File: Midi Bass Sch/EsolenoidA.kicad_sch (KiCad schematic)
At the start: 105 parts, among them Q10 BDW93C, Q11 BDW93C, Q12 BDW93C, Q13 BDW93C, Q14 BDW93C, Q15 BDW93C, Q16 BDW93C, Q17 BDW93C, Q18 BDW93C, Q19 BDW93C, Q20 BDW93C, Q21 BDW93C, Q22 BDW93C, Q23 BDW93C, Q24 BDW93C, Q25 BDW93C, Q26 BDW93C, Q27 BDW93C, Q28 BDW93C, Q9 BDW93C, U10 LTV-247, U11 LTV-247, U12 LTV-247, U13 LTV-247, U9 LTV-247

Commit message: working on troubleshooting section of report
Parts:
- renumbered L9 to L13, L10 to L14, L11 to L15, L12 to L16, L13 to L17, L14 to L18, L15 to L19, L16 to L20, L17 to L21, L18 to L22, L19 to L23, L20 to L24, L21 to L25, L22 to L26, L23 to L27, L24 to L28, L25 to L29, L26 to L30, L27 to L31, L28 to L32, Q9 to Q13, Q10 to Q14, Q11 to Q15, Q12 to Q16, Q13 to Q17, Q14 to Q18, Q15 to Q19, Q16 to Q20, Q17 to Q21, Q18 to Q22, Q19 to Q23, Q20 to Q24, Q21 to Q25, Q22 to Q26, Q23 to Q27, Q24 to Q28, Q25 to Q29, Q26 to Q30, Q27 to Q31, Q28 to Q32, R88 to R100, R89 to R101, R90 to R102, R91 to R103, R92 to R104, R93 to R105, R94 to R106, R95 to R107, R96 to R108, R97 to R109, R98 to R110, R99 to R111, R100 to R112, R101 to R113, R102 to R114, R103 to R115, R104 to R116, R105 to R117, R106 to R118, R107 to R119, R108 to R120, R109 to R121, R110 to R122, R111 to R123, R112 to R124, R113 to R125, R114 to R126, R115 to R127, R116 to R128, R117 to R129, R58 to R70, R59 to R71, R60 to R72, R61 to R73, R62 to R74, R63 to R75, R64 to R76, R65 to R77, R66 to R78, R67 to R79, R68 to R80, R69 to R81, R70 to R82, R71 to R83, R72 to R84, R73 to R85, R74 to R86, R75 to R87, R76 to R88, R77 to R89, R78 to R90, R79 to R91, R80 to R92, R81 to R93, R82 to R94, R83 to R95, R84 to R96, R85 to R97, R86 to R98, R87 to R99, U9 to U11, U10 to U12, U11 to U13, U12 to U14, U13 to U15

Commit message: changed transistor for schematic
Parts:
- Q13, Q14, Q15, Q16, Q17, Q18, Q19, Q20, Q21, Q22, Q23, Q24, Q25, Q26, Q27, Q28, Q29, Q30, Q31, Q32: value BDW93C -> STN851-A
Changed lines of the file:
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@@
 			)
 		)
-		(property "Value" "BDW93C"
+		(property "Value" "STN851-A"
 			(at 119.38 97.7899 0)
 			(effects
@@
 			)
 		)
-		(property "Value" "BDW93C"
+		(property "Value" "STN851-A"
 			(at 119.38 67.3099 0)
 			(effects
@@
 			)
 		)
-		(property "Value" "BDW93C"
+		(property "Value" "STN851-A"
 			(at 118.11 191.7699 0)
 			(effects
@@
 			)
 		)
-		(property "Value" "BDW93C"
+		(property "Value" "STN851-A"
 			(at 172.72 132.0799 0)
 			(effects
@@
 			)
 		)
-		(property "Value" "BDW93C"
+		(property "Value" "STN851-A"
 			(at 64.77 35.5599 0)
 			(effects
@@
 			)
 		)
-		(property "Value" "BDW93C"
+		(property "Value" "STN851-A"
 			(at 172.72 99.0599 0)
 			(effects
@@
 			)
 		)
-		(property "Value" "BDW93C"
+		(property "Value" "STN851-A"
 			(at 236.22 68.5799 0)
 			(effects
@@
 			)
 		)
-		(property "Value" "BDW93C"
+		(property "Value" "STN851-A"
 			(at 62.23 132.0799 0)
 			(effects
@@
 			)
 		)
-		(property "Value" "BDW93C"
+		(property "Value" "STN851-A"
 			(at 118.11 128.2699 0)
 			(effects
@@
 			)
 		)
-		(property "Value" "BDW93C"
+		(property "Value" "STN851-A"
 			(at 119.38 35.5599 0)
 			(effects
@@
 			)
 		)
-		(property "Value" "BDW93C"
+		(property "Value" "STN851-A"
 			(at 172.72 36.8299 0)
 			(effects
@@
 			)
 		)
-		(property "Value" "BDW93C"
+		(property "Value" "STN851-A"
 			(at 118.11 161.2899 0)
 			(effects
@@
 			)
 		)
-		(property "Value" "BDW93C"
+		(property "Value" "STN851-A"
 			(at 237.49 133.3499 0)
 			(effects
@@
 			)
 		)
-		(property "Value" "BDW93C"
+		(property "Value" "STN851-A"
 			(at 172.72 68.5799 0)
 			(effects
@@
 			)
 		)
-		(property "Value" "BDW93C"
+		(property "Value" "STN851-A"
 			(at 236.22 36.8299 0)
 			(effects
@@
 			)
 		)
-		(property "Value" "BDW93C"
+		(property "Value" "STN851-A"
 			(at 62.23 100.3299 0)
 			(effects
@@
 			)
 		)
-		(property "Value" "BDW93C"
+		(property "Value" "STN851-A"
 			(at 63.5 68.5799 0)
 			(effects
@@
 			)
 		)
-		(property "Value" "BDW93C"
+		(property "Value" "STN851-A"
 			(at 236.22 99.0599 0)
 			(effects
@@
 			)
 		)
-		(property "Value" "BDW93C"
+		(property "Value" "STN851-A"
 			(at 62.23 163.8299 0)
 			(effects
@@
 			)
 		)
-		(property "Value" "BDW93C"
+		(property "Value" "STN851-A"
 			(at 60.96 194.3099 0)
 			(effects

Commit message: began getting images for schematic appendix
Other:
- title: (none) -> E-slave Solenoid Array
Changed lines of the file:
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@@
 	(generator_version "8.0")
 	(paper "A")
+	(title_block
+		(title "E-slave Solenoid Array")
+		(date "2024-12-10")
+		(rev "A")
+	)
 	(junction
 		(at 233.68 54.61)

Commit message: began working on pcb layout deleted extra schematics for solenoid break out board
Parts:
- L13, L14, L15, L16, L17, L18, L19, L20, L21, L22, L23, L24, L25, L26, L27, L28, L29, L30, L31, L32: footprint (none) -> Connector_PinHeader_2.54mm:PinHeader_1x02_P2.54mm_Vertical

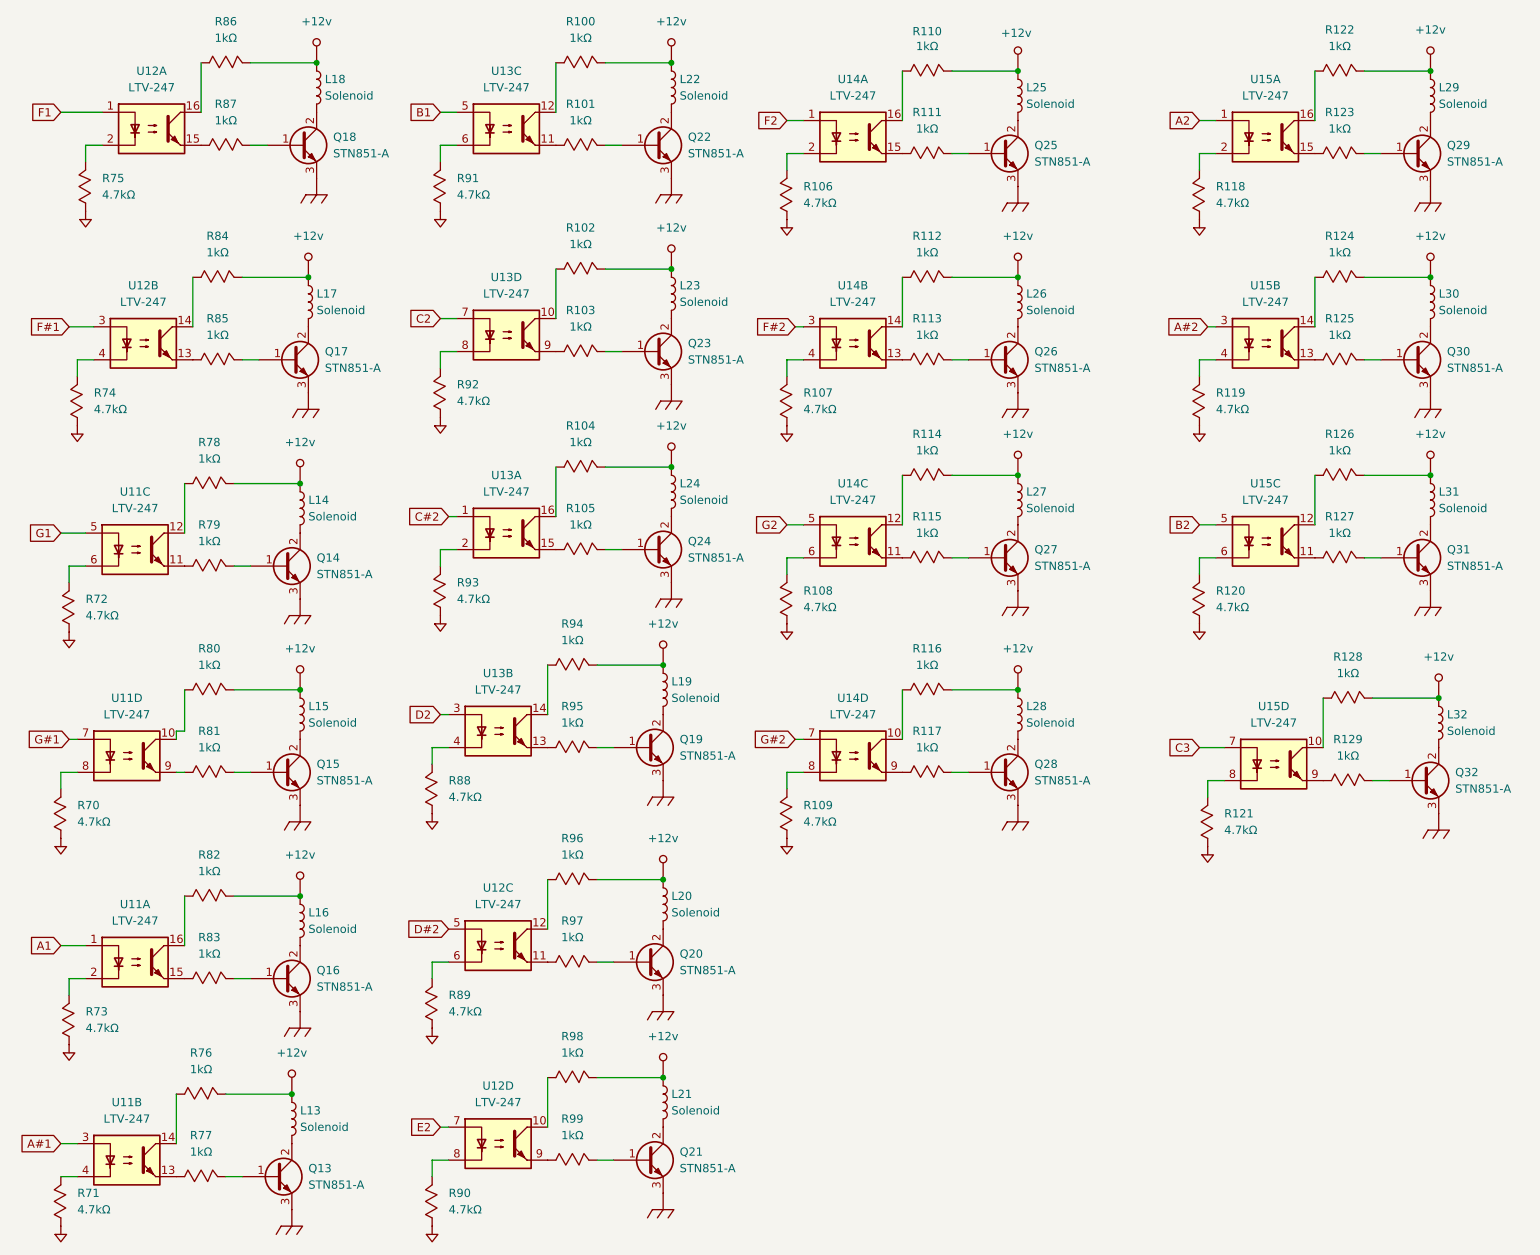
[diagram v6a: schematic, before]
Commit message: changed solenoid schematic to include LED indicators
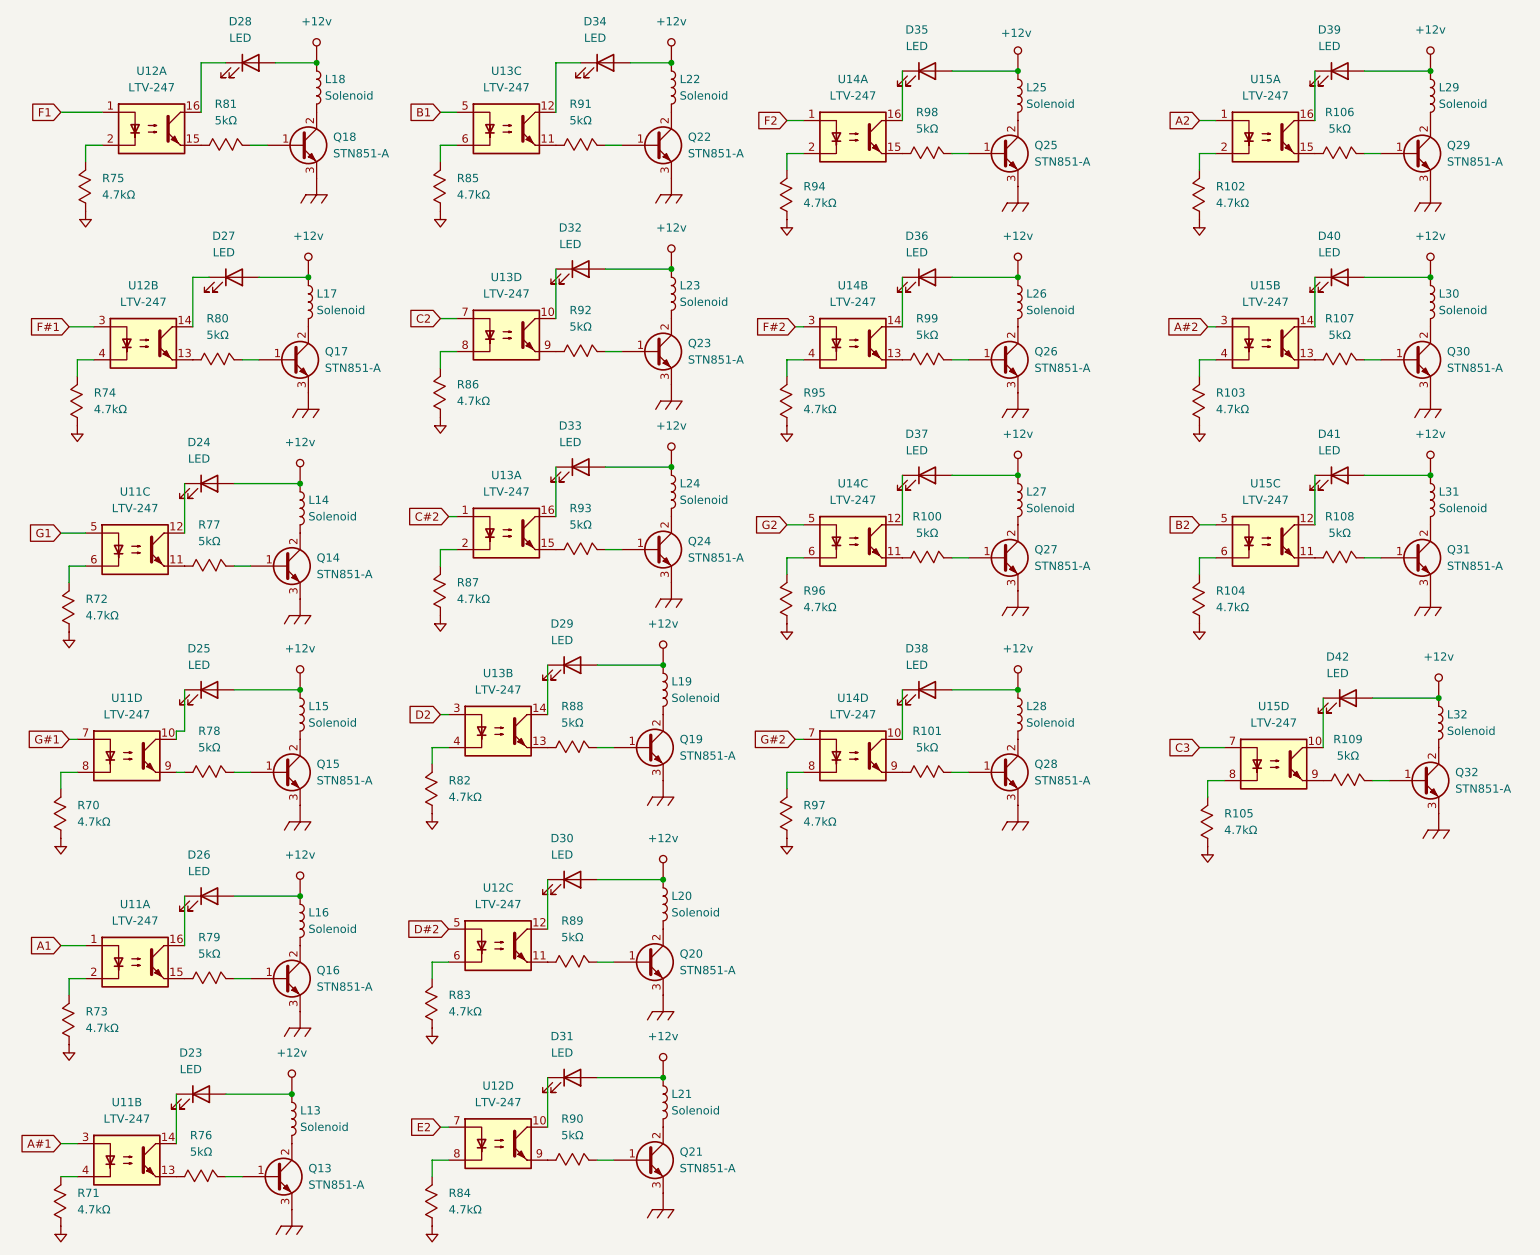
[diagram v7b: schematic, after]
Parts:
- removed R100, R102, R104, R110, R112, R114, R116, R122, R124, R126, R128, R76, R78, R80, R82, R84, R86, R94, R96, R98: 1kΩ, Resistor_SMD:R_0805_2012Metric_Pad1.20x1.40mm_HandSolder, symbol Custom Symbols:Resistor_Mod
- added D23, D24, D25, D26, D27, D28, D29, D30, D31, D32, D33, D34, D35, D36, D37, D38, D39, D40, D41, D42: LED, symbol Device:LED
- R100: renamed from R115; value 1kΩ -> 5kΩ
- R101: renamed from R117; value 1kΩ -> 5kΩ
- R106: renamed from R123; value 1kΩ -> 5kΩ
- R107: renamed from R125; value 1kΩ -> 5kΩ
- R108: renamed from R127; value 1kΩ -> 5kΩ
- R109: renamed from R129; value 1kΩ -> 5kΩ
- R76: renamed from R77; value 1kΩ -> 5kΩ
- R77: renamed from R79; value 1kΩ -> 5kΩ
- R78: renamed from R81; value 1kΩ -> 5kΩ
- R79: renamed from R83; value 1kΩ -> 5kΩ
- R80: renamed from R85; value 1kΩ -> 5kΩ
- R81: renamed from R87; value 1kΩ -> 5kΩ
- R88: renamed from R95; value 1kΩ -> 5kΩ
- R89: renamed from R97; value 1kΩ -> 5kΩ
- R90: renamed from R99; value 1kΩ -> 5kΩ
- R91: renamed from R101; value 1kΩ -> 5kΩ
- R92: renamed from R103; value 1kΩ -> 5kΩ
- R93: renamed from R105; value 1kΩ -> 5kΩ
- R98: renamed from R111; value 1kΩ -> 5kΩ
- R99: renamed from R113; value 1kΩ -> 5kΩ
- renumbered R118 to R102, R119 to R103, R120 to R104, R121 to R105, R88 to R82, R89 to R83, R90 to R84, R91 to R85, R92 to R86, R93 to R87, R106 to R94, R107 to R95, R108 to R96, R109 to R97
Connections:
- net +12v: now also D23.2 (A), D24.2 (A), D25.2 (A), D26.2 (A), D27.2 (A), D28.2 (A), D29.2 (A), D30.2 (A), D31.2 (A), D32.2 (A), D33.2 (A), D34.2 (A), D35.2 (A), D36.2 (A), D37.2 (A), D38.2 (A), D39.2 (A), D40.2 (A), D41.2 (A), D42.2 (A)
- net at U14.10: now also D38.1 (K)
- net at U11.14: now also D23.1 (K)
- net at U13.16: now also D33.1 (K)
- net at U14.12: now also D37.1 (K)
- net at U11.16: now also D26.1 (K)
- net at U13.10: now also D32.1 (K)
- net at U15.14: now also D40.1 (K)
- net at U12.16: now also D28.1 (K)
- net at U12.12: now also D30.1 (K)
- net at U11.10: now also D25.1 (K)
- net at U14.16: now also D35.1 (K)
- net at U12.10: now also D31.1 (K)
- net at U12.14: now also D27.1 (K)
- net at U15.16: now also D39.1 (K)
- net at U13.12: now also D34.1 (K)
- net at U14.14: now also D36.1 (K)
- net at U13.14: now also D29.1 (K)
- net at U11.12: now also D24.1 (K)
- net at U15.12: now also D41.1 (K)
- net at U15.10: now also D42.1 (K)

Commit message: created pcb for breakout working on pcb for main control board
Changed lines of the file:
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@@
 (kicad_sch
-	(version 20231120)
+	(version 20250114)
 	(generator "eeschema")
-	(generator_version "8.0")
+	(generator_version "9.0")
 	(paper "A")
 	(title_block
